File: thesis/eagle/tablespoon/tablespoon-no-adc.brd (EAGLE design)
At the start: 103.2 x 68.6 mm, 29 parts, among them IC1 7805DT, IC2 7805DT, IC3 TL072D, U1 ADCS7477, U2 ADCS7477

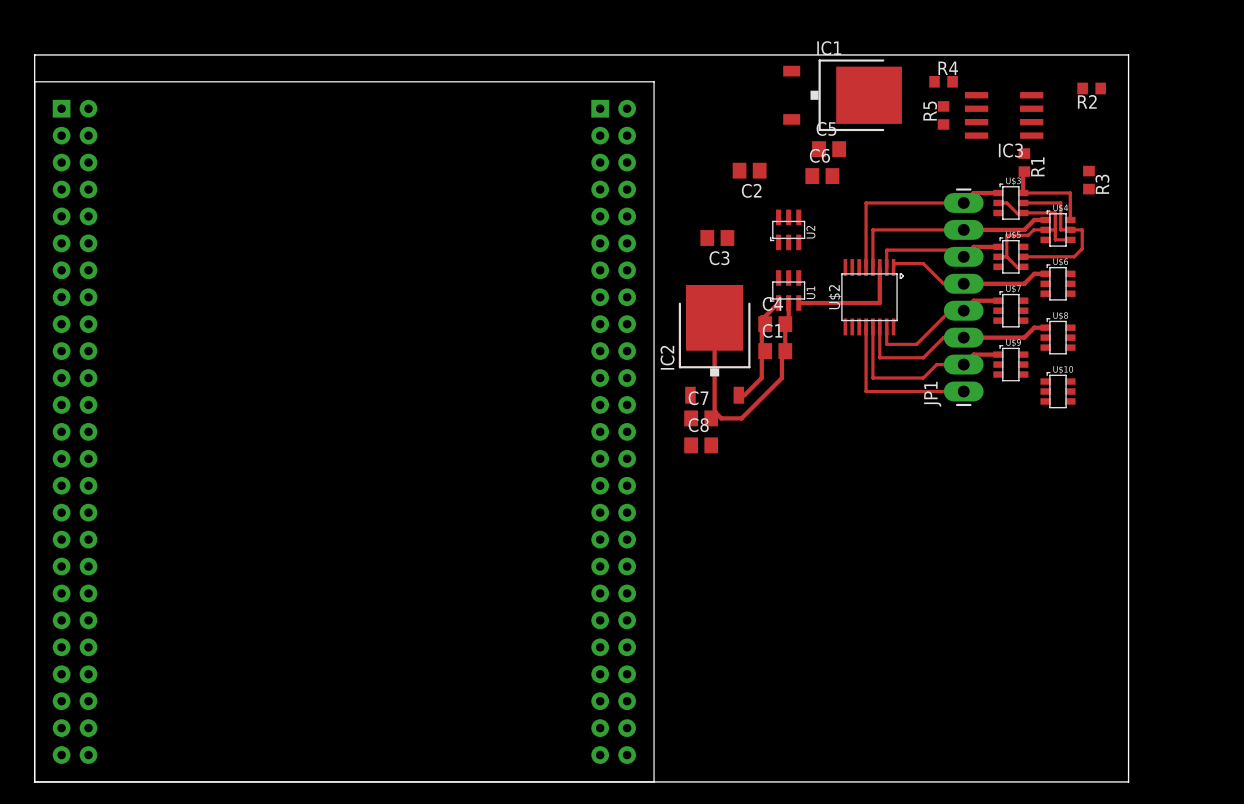
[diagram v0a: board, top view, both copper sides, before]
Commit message: working on 8-channel DAC side
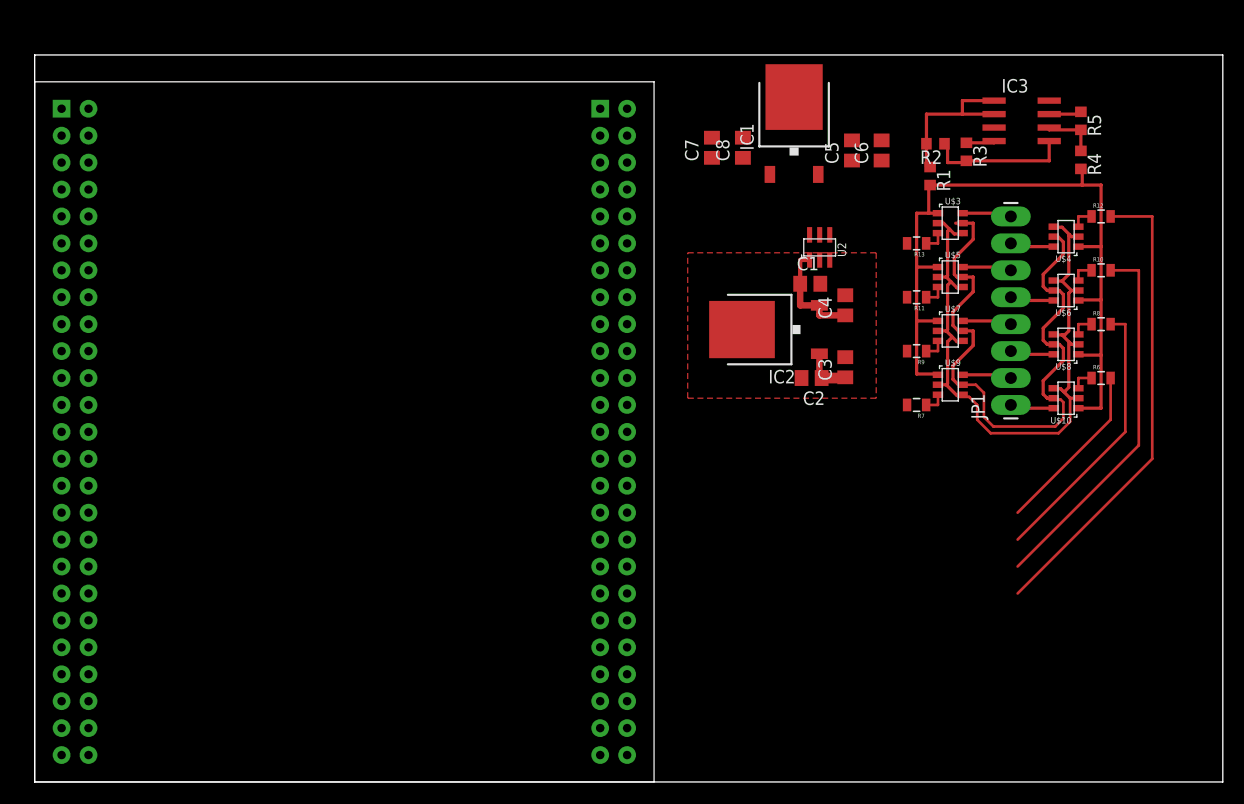
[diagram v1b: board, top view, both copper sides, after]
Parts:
- removed U$2: 4051", butter:TSSOP-16
- removed U1: ADCS7477, butter:SOT-23-6
- added R10, R11, R12, R13, R6, R7, R8, R9: (no value), SparkFun-Passives:0805
- moved C8 28.3 mm to (66.8, 59.8), turned to 90 degrees
- moved C7 25.5 mm to (63.9, 59.8), turned to 90 degrees
- moved C2 20.4 mm to (73.3, 38.1)
- moved C3 17.2 mm to (76.5, 39.1), turned to 90 degrees
- moved R2 15.6 mm to (85.0, 60.2)
- moved R4 14.9 mm to (98.7, 58.7), turned to 270 degrees
- moved R5 13.0 mm to (98.7, 62.4), turned to 270 degrees
- moved R3 11.9 mm to (87.9, 59.4)
- moved R1 8.98 mm to (84.5, 57.1)
- moved C1 7.16 mm to (73.2, 47.0)
- moved C4 6.84 mm to (76.5, 45.0), turned to 90 degrees
- moved C6 6.09 mm to (79.9, 59.6), turned to 90 degrees
- moved U$3 6.02 mm to (86.4, 52.7)
- moved U$5 6.02 mm to (86.4, 47.6)
- moved U$7 6.02 mm to (86.4, 42.5)
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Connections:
- net N$7 renamed 4.6V
- removed net N$1: U$2.P$3, U1.P$3
- removed net N$3: C1.2, C2.2, C3.2, C4.2, IC2.3, U1.P$2, U2.P$2
- new net N$15: R8.1, U$8.P$3
- new net N$17: R9.1, U$7.P$3
- new net N$18: R12.1, U$4.P$3
- new net N$19: R13.1, U$3.P$3
- new net N$20: R11.1, U$5.P$3
- new net N$21: R10.1, U$6.P$3
- new net N$4: R6.1, U$10.P$3
- new net N$7: R7.1, U$9.P$3
- net !CS: no longer U1.P$6
- net 5V: no longer U$2.P$16
- net CK: no longer U1.P$4
- net D0: no longer U1.P$5
- net GND: now also C1.2, C2.2, C3.2, C4.2, IC2.3, U2.P$2; no longer U$2.P$7, U$2.P$8
- net N$10: now also U$8.P$6; no longer U$2.P$14, U$8.P$1
- net N$11: now also U$10.P$6; no longer U$10.P$1, U$2.P$12
- net N$12: now also U$9.P$6; no longer U$2.P$13, U$9.P$1
- net N$16: now also U$10.P$1, U$3.P$1, U$4.P$1, U$5.P$1, U$6.P$1, U$7.P$1, U$8.P$1, U$9.P$1; no longer U$10.P$6, U$3.P$6, U$4.P$6, U$5.P$6, U$6.P$6, U$7.P$6, U$8.P$6, U$9.P$6
- net N$2: no longer U1.P$1
- net N$27: now also U$5.P$6; no longer U$2.P$2, U$5.P$1
- net N$28: now also U$4.P$6; no longer U$2.P$4, U$4.P$1
- net N$29: now also U$3.P$6; no longer U$2.P$5, U$3.P$1
- net N$6: now also U$7.P$6; no longer U$2.P$15, U$7.P$1
- net N$9: now also U$6.P$6; no longer U$2.P$1, U$6.P$1
- net S0: no longer U$2.P$11
- net S1: no longer U$2.P$10
- net S2: no longer U$2.P$9
- net SE: no longer U$2.P$6
- net SW1: now also R6.2; no longer U$10.P$3
- net SW2: now also R7.2; no longer U$9.P$3
- net SW3: now also R8.2; no longer U$8.P$3
- net SW4: now also R9.2; no longer U$7.P$3
- net SW5: now also R10.2; no longer U$6.P$3
- net SW6: now also R11.2; no longer U$5.P$3
- net SW7: now also R12.2; no longer U$4.P$3
- net SW8: now also R13.2; no longer U$3.P$3
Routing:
- net N$16: track 9.05 -> 73.6 mm
- net GND: track 19.3 -> 70.4 mm
- net 4.6V: track 15.8 -> 64.8 mm
- net SW7: track 0.00 -> 44.7 mm
- net SW5: track 0.00 -> 35.3 mm
- net SW3: track 0.00 -> 25.9 mm
- net N$3: track 24.6 -> 0.00 mm
- net SW1: track 0.00 -> 16.3 mm
- net N$28: track 20.2 -> 4.17 mm
- net N$8: track 0.00 -> 16.0 mm
- net N$10: track 19.7 -> 4.17 mm
- net N$29: track 19.0 -> 4.79 mm
- net N$13: track 0.00 -> 13.7 mm
- net N$12: track 17.6 -> 4.79 mm
- net N$9: track 15.9 -> 4.17 mm
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- added copper zone on layer 1, net GND
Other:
- board size 103.2 x 68.6 mm -> 112.1 x 68.6 mm

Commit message: driving tablespoon
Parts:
- moved R5 22.5 mm to (78.9, 51.7), turned to 180 degrees
- moved R4 19.7 mm to (79.5, 54.0), turned to 0 degrees
- moved IC3 14.4 mm to (78.9, 59.9), turned to 180 degrees
- moved R3 13.1 mm to (75.6, 54.9), turned to 90 degrees
- moved R2 10.2 mm to (74.9, 58.3), turned to 90 degrees
- moved C6 8.17 mm to (74.0, 65.3)
- moved C5 7.73 mm to (71.9, 65.3)
- moved C8 7.32 mm to (62.2, 65.5)
- moved C7 6.94 mm to (59.9, 65.5)
- moved IC1 5.23 mm to (67.1, 64.6)
- moved IC2 1.27 mm to (67.9, 42.7)
- moved C1 1.27 mm to (71.9, 47.0)
- moved C2 1.27 mm to (72.0, 38.1)
- moved C3 1.27 mm to (75.2, 39.1)
- moved C4 1.27 mm to (75.2, 45.0)
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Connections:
- net !CS: now also U2.P$6
- net CK: now also U2.P$4
- net SW1: now also R11.2, U$1.P$60; no longer R6.2, U$1.P$20
- net SW2: now also R13.2, U$1.P$59; no longer R7.2, U$1.P$19
- net SW3: now also R12.2; no longer R8.2
- net SW4: now also R10.2; no longer R9.2
- net SW5: now also R8.2; no longer R10.2
- net SW6: now also R6.2; no longer R11.2
- net SW7: now also R7.2; no longer R12.2
- net SW8: now also R9.2; no longer R13.2
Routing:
- net DAC: track 0.00 -> 83.5 mm
- net CK: track 0.00 -> 81.3 mm
- net SW4: track 0.00 -> 78.4 mm
- net SW2: track 0.00 -> 70.6 mm
- net SW3: track 25.9 -> 91.5 mm
- net SW6: track 0.00 -> 62.9 mm
- net SW1: track 16.3 -> 76.9 mm
- net SW8: track 0.00 -> 41.6 mm
- net SW5: track 35.3 -> 73.7 mm
- net D1: track 0.00 -> 30.6 mm
- net !CS: track 0.00 -> 16.3 mm
- net N$5: track 4.63 -> 18.0 mm
- net 5V: track 0.00 -> 11.8 mm
- net CUR: track 3.20 -> 14.2 mm
- net N$13: track 13.7 -> 3.88 mm
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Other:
- board size 112.1 x 68.6 mm -> 106.3 x 71.1 mm
